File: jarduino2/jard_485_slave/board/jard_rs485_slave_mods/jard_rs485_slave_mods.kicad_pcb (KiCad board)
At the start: 2 copper layers, 81 x 66 mm, 24 parts, among them J1 NETWORK IN, J2 NETWORK OUT, J4 LED, J5 Niveau bas, J6 Electrovanne 12V, J7 Niveau Haut, Q1 TIP41C, U1 BPC_Mod485

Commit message: Carte en L
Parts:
- removed the REF** at (136.0, 125.0)
- removed the REF** at (136.0, 69.0)
- removed the REF** at (65.0, 125.0)
- removed the REF** at (65.0, 69.0)
- added REF**: BPC_Trou4mm_Fixation, bpc:BPC_Trou4mm_Fixation, F.Cu at (141.0, 117.0)
- moved R1 126.1 mm to (197.0, 102.0)
- moved J4 119.5 mm to (196.0, 93.0), turned to 270 degrees
- moved R2 103.8 mm to (188.0, 93.0), turned to 180 degrees
- moved R5 95.5 mm to (190.0, 52.0)
- moved C7 83.7 mm to (188.0, 101.0)
- moved U1 81.9 mm to (154.0, 119.0), turned to 90 degrees
- moved J5 78.6 mm to (192.0, 65.0)
- moved C5 77.1 mm to (175.0, 102.0)
- moved R4 76.6 mm to (185.0, 48.0)
- moved R3 75.3 mm to (179.0, 48.0), turned to 180 degrees
- moved R6 75.3 mm to (192.0, 84.0), turned to 180 degrees
- moved C12 75.1 mm to (190.0, 35.0)
- moved A1 71.1 mm to (182.0, 95.0)
- moved Q1 69.4 mm to (177.0, 36.0), turned to 270 degrees
- moved J7 65.3 mm to (192.0, 77.0)
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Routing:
- net Vcc: track 68.6 -> 151.4 mm
- net CMD_EV: track 8.74 -> 36.0 mm
- net Net-(A1-Pad30): track 173.8 -> 199.5 mm
- net Net-(A1-Pad8): track 41.6 -> 18.5 mm
- net IN_LVL_LOW: track 49.4 -> 27.9 mm
- net RX: track 41.8 -> 61.0 mm
- net Net-(D1-Pad2): track 41.4 -> 24.8 mm
- net TX: track 51.4 -> 34.9 mm
- net IN_LVL_HIGH: track 34.6 -> 24.7 mm
- net Net-(J1-Pad2): track 56.8 -> 53.9 mm
- net TXEN: track 67.1 -> 69.9 mm, vias 0 -> 1
- net Net-(Q1-Pad1): track 23.8 -> 22.2 mm
- net Net-(J1-Pad3): track 56.7 -> 57.7 mm
- net Net-(J6-Pad1): track 7.19 -> 6.64 mm
- removed copper zone on F.Cu, net GND
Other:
- board size 81 x 66 mm -> 98 x 94 mm
- board text removed: "+"
- board text removed: "-"
- board text removed: "1"
- board text removed: "BUS J1 et J2: 1- Pow 12V 2- A 3- B 4- Gnd"
- board text removed: "Cmd EV"
- board text removed: "Niv Bas"
- board text removed: "Niv Haut"
- board text removed: "OYA 485 Rev A0 BPC 2023"

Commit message: ?
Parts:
- added REF**: BPC_Trou4mm_Fixation, bpc:BPC_Trou4mm_Fixation, F.Cu at (179.0, 37.0)
- U1: value BPC_Mod485 -> Arduino_Mod_RS485
- moved J2 70.1 mm to (188.0, 121.0), turned to 90 degrees
- moved Q1 51.4 mm to (183.0, 87.0)
- moved R4 50.0 mm to (186.0, 98.0), turned to 180 degrees
- moved D1 48.5 mm to (179.0, 110.0), turned to 270 degrees
- moved R3 47.3 mm to (190.0, 94.0), turned to 90 degrees
- moved R1 45.5 mm to (152.0, 109.0), turned to 180 degrees
- moved J6 45.3 mm to (188.0, 79.0), turned to 90 degrees
- moved J4 42.2 mm to (157.0, 109.0), turned to 90 degrees
- moved J7 41.0 mm to (192.0, 36.0), turned to 180 degrees
- moved R6 37.0 mm to (191.0, 47.0), turned to 90 degrees
- moved U1 36.7 mm to (121.0, 103.0)
- moved J5 35.8 mm to (171.0, 36.0), turned to 180 degrees
- moved C11 29.0 mm to (189.0, 67.0), turned to 180 degrees
- moved R2 28.8 mm to (164.0, 109.0), turned to 0 degrees
- moved C12 22.0 mm to (191.0, 57.0), turned to 180 degrees
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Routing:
- net Net-(J1-Pad3): track 57.7 -> 143.6 mm
- net Net-(A1-Pad30): track 199.5 -> 115.4 mm
- net Net-(D1-Pad2): track 24.8 -> 94.0 mm
- net Net-(J1-Pad2): track 53.9 -> 105.0 mm, vias 0 -> 1
- net RX: track 61.0 -> 22.3 mm
- net Net-(A1-Pad8): track 18.5 -> 50.4 mm, vias 0 -> 1
- net Vcc: track 151.4 -> 125.5 mm
- net IN_LVL_LOW: track 27.9 -> 45.6 mm
- net IN_LVL_HIGH: track 24.7 -> 38.0 mm
- net CMD_EV: track 36.0 -> 26.9 mm
- net Net-(J6-Pad1): track 6.64 -> 14.1 mm
- net TXEN: track 69.9 -> 63.8 mm
- net Net-(Q1-Pad1): track 22.2 -> 17.1 mm
- net TX: track 34.9 -> 30.8 mm
- net Net-(J4-Pad2): track 5.46 -> 4.46 mm
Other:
- board size 98 x 94 mm -> 94 x 94 mm
- board text added: "Bas"
- board text added: "Bus 485 J1/J2 1- Pwr 12V 2- A 3- B 4- GND"
- board text added: "Carte Commande OYA BPC 2023 Rev A0"
- board text added: "Cmd EV"
- board text added: "Haut"
- board text added: "LED"

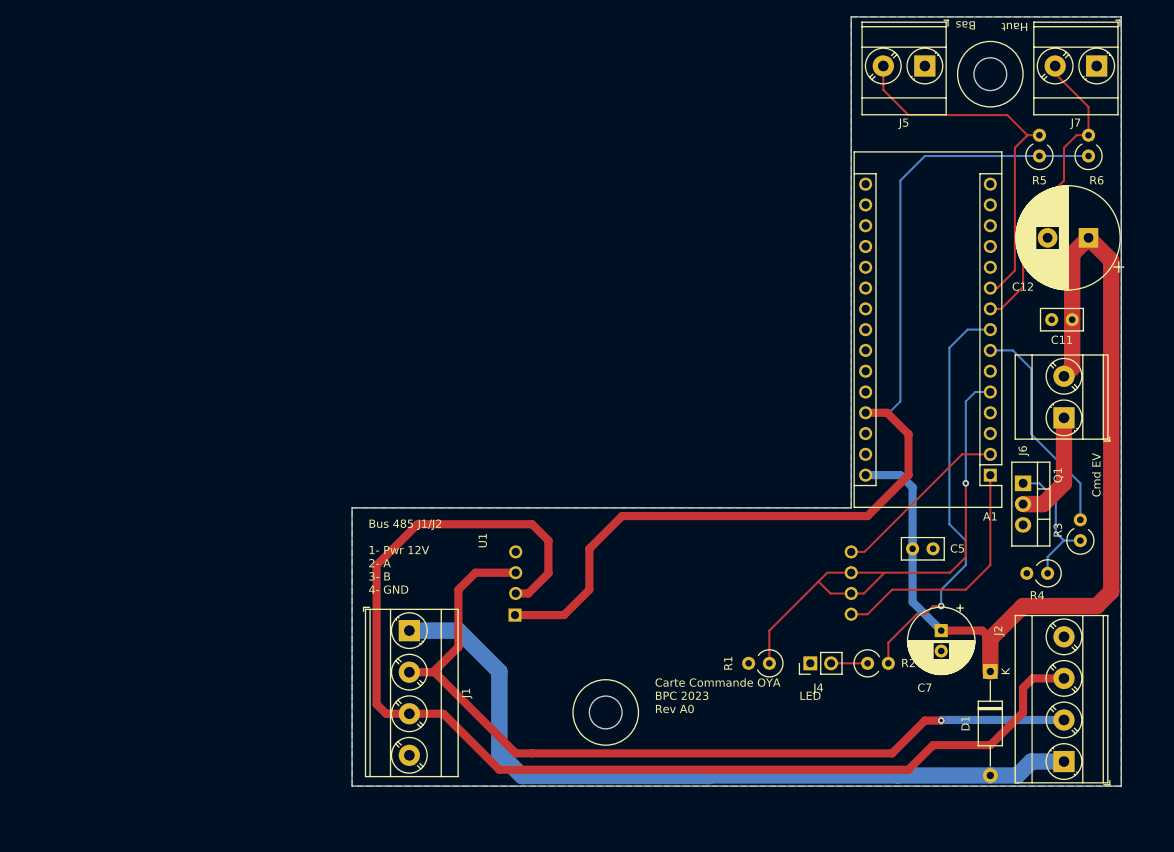
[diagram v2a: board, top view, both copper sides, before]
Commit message: Redesign avec 1 MOS et 2 entrées flowmeter Dimensions ajustées suite proto mécanique Ajout datasheets
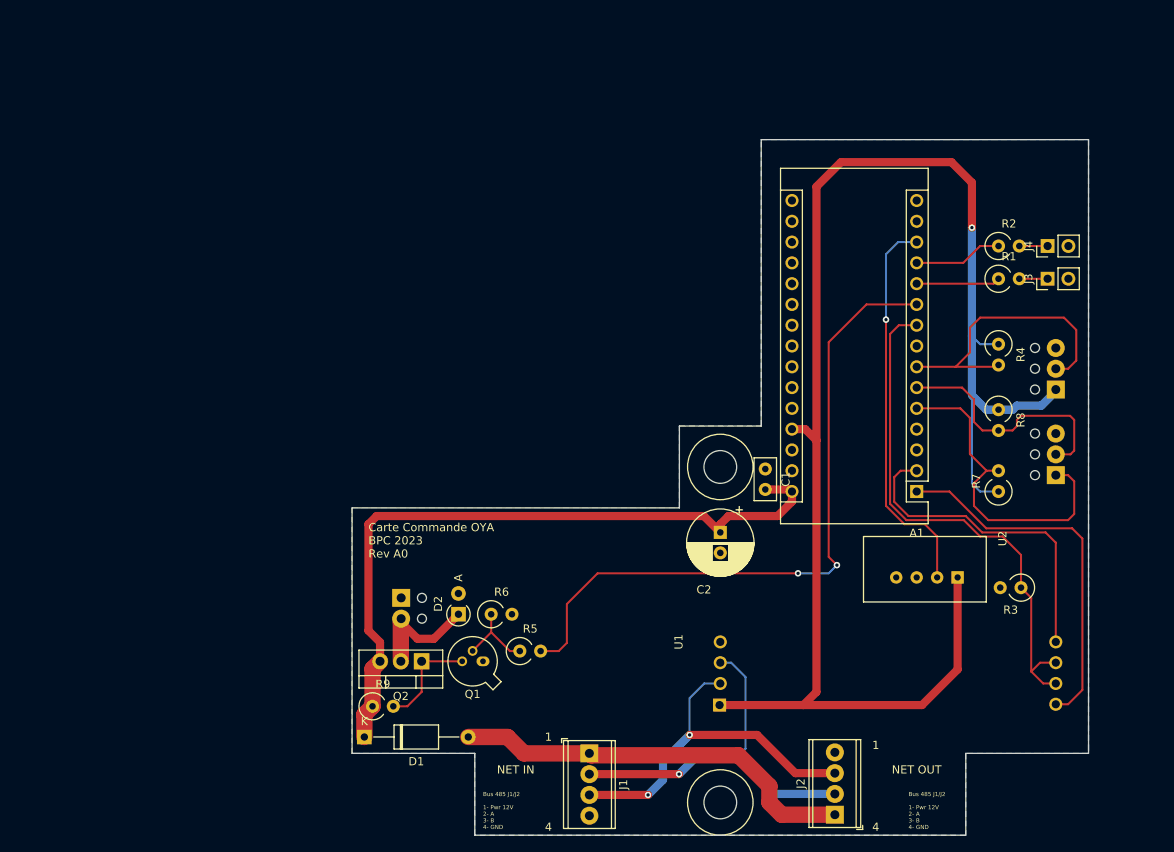
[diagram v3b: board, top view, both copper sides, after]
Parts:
- removed C11: 10nF, Capacitor_THT:C_Disc_D5.0mm_W2.5mm_P2.50mm
- removed C12: 20µF, Capacitor_THT:CP_Radial_D12.5mm_P5.00mm
- removed C5: 10n, Capacitor_THT:C_Disc_D5.0mm_W2.5mm_P2.50mm
- removed the J7 at (192.0, 36.0)
- added C1: 10n, Capacitor_THT:C_Disc_D5.0mm_W2.5mm_P2.50mm, F.Cu at (151.5, 85.2)
- added D2: D, Diode_THT:D_A-405_P2.54mm_Vertical_AnodeUp, F.Cu at (114.0, 103.0)
- added J3: LED, Connector_PinHeader_2.54mm:PinHeader_1x02_P2.54mm_Vertical, F.Cu at (186.0, 62.0)
- added J6: Niveau, TerminalBlock_Phoenix:TerminalBlock_Phoenix_MPT-0,5-3-2.54_1x03_P2.54mm_Horizontal, B.Cu at (187.0, 86.0)
- added Q2: P03P4L-04, Package_TO_SOT_THT:TO-220-3_Vertical, F.Cu at (109.5, 108.8)
- added R7: 100k, Resistor_THT:R_Axial_DIN0309_L9.0mm_D3.2mm_P2.54mm_Vertical, F.Cu at (180.0, 88.0)
- added R8: 100k, Resistor_THT:R_Axial_DIN0309_L9.0mm_D3.2mm_P2.54mm_Vertical, F.Cu at (180.0, 78.0)
- added R9: 100k, Resistor_THT:R_Axial_DIN0309_L9.0mm_D3.2mm_P2.54mm_Vertical, F.Cu at (103.5, 114.2)
- added U2: BPC_DHT22, bpc:BPC_DHT22, F.Cu at (175.0, 98.5)
- J1, J2: footprint TerminalBlock_Phoenix:TerminalBlock_Phoenix_MKDS-3-4-5.08_1x04_P5.08mm_Horizontal -> TerminalBlock_Phoenix:TerminalBlock_Phoenix_MPT-0,5-4-2.54_1x04_P2.54mm_Horizontal
- J5: value Niveau bas -> Debit; footprint TerminalBlock_Phoenix:TerminalBlock_Phoenix_MKDS-3-2-5.08_1x02_P5.08mm_Horizontal -> TerminalBlock_Phoenix:TerminalBlock_Phoenix_MPT-0,5-3-2.54_1x03_P2.54mm_Horizontal; moved to B.Cu
- J7: renamed from J6; footprint TerminalBlock_Phoenix:TerminalBlock_Phoenix_MKDS-3-2-5.08_1x02_P5.08mm_Horizontal -> TerminalBlock_Phoenix:TerminalBlock_Phoenix_MPT-0,5-2-2.54_1x02_P2.54mm_Horizontal; moved to B.Cu
- Q1: value TIP41C -> BPC_2N2222A; footprint Package_TO_SOT_THT:TO-220-3_Vertical -> Package_TO_SOT_THT:TO-18-3
- R1: value 100k -> 150
- R3: value 50 -> 100k
- R5: value 100k -> 100
- U1: value Arduino_Mod_RS485 -> BPC_Mod485
- moved REF** 94.9 mm to (146.0, 126.0)
- moved R6 92.0 mm to (118.0, 103.0), turned to 0 degrees
- moved R5 87.7 mm to (121.5, 107.5), turned to 0 degrees
- moved J7 83.9 mm to (107.0, 101.0), turned to 270 degrees
- moved D1 76.9 mm to (102.5, 118.0), turned to 0 degrees
- moved Q1 69.5 mm to (117.0, 108.8), turned to 180 degrees
- moved J4 58.7 mm to (186.0, 58.0)
- moved R1 54.7 mm to (180.0, 62.0), turned to 0 degrees
- moved R2 53.5 mm to (180.0, 58.0)
- moved J5 42.7 mm to (187.0, 75.5), turned to 90 degrees
- moved REF** 33.1 mm to (146.0, 85.0)
- moved C2 29.5 mm to (146.0, 93.0)
- moved J2 28.7 mm to (160.0, 127.5)
- moved R4 28.6 mm to (180.0, 70.0), turned to 270 degrees
- moved U1 27.3 mm to (146.0, 114.0)
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- renumbered C7 to C2
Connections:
- A1 pad 10: IN_LVL_LOW -> CMD_EV
- A1 pad 11: Net-(A1-Pad11) -> LED1
- A1 pad 12: Net-(A1-Pad12) -> LED2
- A1 pad 13: Net-(A1-Pad13) -> TEMP
- A1 pad 5: TXEN -> IN_LVL_LOW
- A1 pad 6: Net-(A1-Pad6) -> IN_LVL_HIGH
- A1 pad 7: CMD_EV -> FLOW_IN
- A1 pad 9: IN_LVL_HIGH -> TXEN
- J1 pad 4: Net-(J1-Pad4) -> GND
- J2 pad 4: Net-(J1-Pad4) -> GND
- J4 pad 1: GND -> Net-(J4-Pad1)
- J4 pad 2: Net-(J4-Pad2) -> GND
- J5 pad 1: GND -> Vcc
- J5 pad 2: IN_LVL_LOW -> FLOW_IN
- J7 pad 1: Net-(J6-Pad1) -> GND
- J7 pad 2: Net-(A1-Pad30) -> Net-(D2-Pad1)
- Q1 pad 1: Net-(Q1-Pad1) -> GND
- Q1 pad 2: Net-(J6-Pad1) -> Net-(Q1-Pad2)
- Q1 pad 3: GND -> Net-(Q1-Pad3)
- R1 pad 1: TXEN -> LED1
- R1 pad 2: GND -> Net-(J3-Pad1)
- R2 pad 1: Net-(J4-Pad2) -> LED2
- R2 pad 2: Net-(A1-Pad8) -> Net-(J4-Pad1)
- R3 pad 1: Net-(Q1-Pad1) -> TXEN
- R3 pad 2: CMD_EV -> GND
- R4 pad 1: Net-(Q1-Pad1) -> Vcc
- R4 pad 2: GND -> FLOW_IN
- R5 pad 1: Vcc -> Net-(Q1-Pad2)
- R5 pad 2: IN_LVL_LOW -> CMD_EV
- R6 pad 1: Vcc -> Net-(Q1-Pad2)
- R6 pad 2: IN_LVL_HIGH -> GND
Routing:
- net Net-(J1-Pad3): track 143.6 -> 45.3 mm, vias 0 -> 2
- net Vcc: track 125.5 -> 187.4 mm, vias 0 -> 1
- net Net-(J1-Pad2): track 105.0 -> 46.8 mm
- net CMD_EV: track 26.9 -> 83.7 mm, vias 0 -> 2
- net Net-(A1-Pad8): track 50.4 -> 0.00 mm, vias 1 -> 0
- net TEMP: track 0.00 -> 47.9 mm, vias 0 -> 1
- net Net-(D1-Pad2): track 94.0 -> 49.9 mm
- net FLOW_IN: track 0.00 -> 36.4 mm
- net Net-(A1-Pad30): track 115.4 -> 87.1 mm
- net RX: track 22.3 -> 40.0 mm
- net Net-(Q1-Pad1): track 17.1 -> 0.00 mm
- net Net-(D2-Pad1): track 0.00 -> 14.4 mm
- net TX: track 30.8 -> 45.1 mm
- net Net-(J6-Pad1): track 14.1 -> 0.00 mm
- net Net-(Q1-Pad3): track 0.00 -> 12.9 mm
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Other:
- board size 94 x 94 mm -> 90 x 85 mm
- board text added: "+"
- board text added: "-"
- board text added: "1"
- board text added: "12V"
- board text added: "4"
- board text added: "Débit"
- board text added: "J5: Débit 1- Vcc 2- Débit/Freq 3- Gnd"
- board text added: "J5: Niveaux 1- Bas 2- Haut 3- Gnd"
- board text added: "NET IN"
- board text added: "NET OUT"
- board text added: "Niveaux"
- board text added: "OUT EV/PMP"
- board text removed: "Bas"
- board text removed: "Cmd EV"
- board text removed: "Haut"
- board text removed: "LED"
